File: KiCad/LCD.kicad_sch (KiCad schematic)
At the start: 4 parts

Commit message: Pulling
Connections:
- net SDA is gone; now on net SCL: R2.2, U3.46 (SDA)
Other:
- moved on the sheet: R3

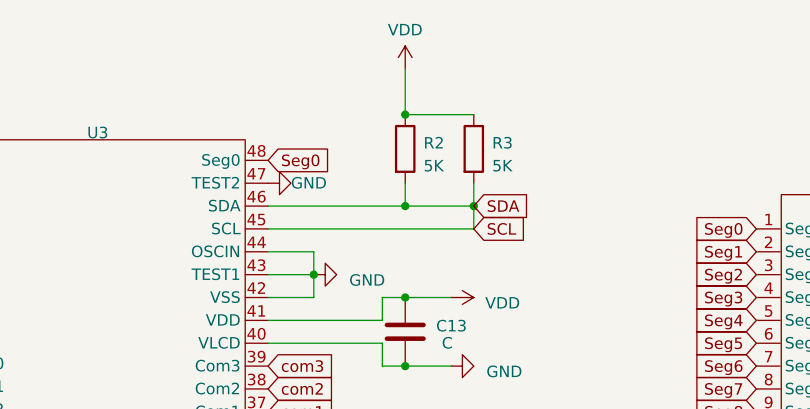
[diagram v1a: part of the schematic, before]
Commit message: Lcd files started.
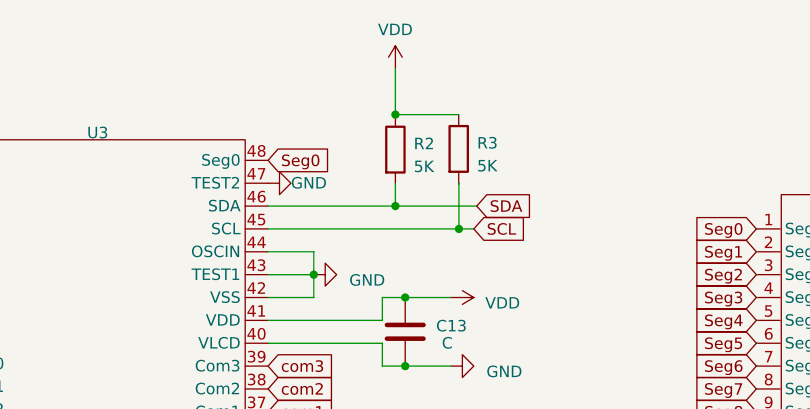
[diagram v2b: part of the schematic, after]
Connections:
- net SCL: no longer R2.2, U3.46 (SDA)
- new net SDA: R2.2, U3.46 (SDA)
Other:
- moved on the sheet: R2, R3
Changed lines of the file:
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@@
     (rev "1.0")
   )
+  (junction (at 125.349 71.12) (diameter 0) (color 0 0 0 0)
+  )
   (junction (at 119.38 78.74) (diameter 0) (color 0 0 0 0)
   )
-  (junction (at 119.38 58.42) (diameter 0) (color 0 0 0 0)
+  (junction (at 118.2878 68.58) (diameter 0) (color 0 0 0 0)
   )
   (junction (at 109.22 76.2) (diameter 0) (color 0 0 0 0)
@@
   (junction (at 119.38 86.36) (diameter 0) (color 0 0 0 0)
   )
-  (junction (at 127 68.58) (diameter 0) (color 0 0 0 0)
-  )
-  (junction (at 119.38 68.58) (diameter 0) (color 0 0 0 0)
+  (junction (at 118.2878 58.42) (diameter 0) (color 0 0 0 0)
   )
   (wire (pts (xy 158.3944 76.2) (xy 158.496 76.2))
@@
     (stroke (width 0) (type default))
   )
-  (wire (pts (xy 127 66.04) (xy 127 68.58))
-    (stroke (width 0) (type default))
-  )
-  (wire (pts (xy 127 68.58) (xy 119.38 68.58))
-    (stroke (width 0) (type default))
-  )
   (wire (pts (xy 158.3944 73.66) (xy 158.496 73.66))
     (stroke (width 0) (type default))
@@
     (stroke (width 0) (type default))
   )
-  (wire (pts (xy 104.14 71.12) (xy 127 71.12))
+  (wire (pts (xy 104.14 71.12) (xy 125.349 71.12))
+    (stroke (width 0) (type default))
+  )
+  (wire (pts (xy 118.2878 58.42) (xy 118.2878 58.4962))
     (stroke (width 0) (type default))
   )
@@
     (stroke (width 0) (type default))
   )
+  (wire (pts (xy 118.2878 58.42) (xy 125.3236 58.42))
+    (stroke (width 0) (type default))
+  )
   (wire (pts (xy 158.3944 104.14) (xy 158.496 104.14))
     (stroke (width 0) (type default))
   )
+  (wire (pts (xy 125.349 71.12) (xy 127 71.12))
+    (stroke (width 0) (type default))
+  )
   (wire (pts (xy 158.3944 86.36) (xy 158.496 86.36))
     (stroke (width 0) (type default))
@@
     (stroke (width 0) (type default))
   )
+  (wire (pts (xy 125.3236 66.0908) (xy 125.3236 66.04))
+    (stroke (width 0) (type default))
+  )
+  (wire (pts (xy 118.2878 53.3146) (xy 118.2878 58.42))
+    (stroke (width 0) (type default))
+  )
   (wire (pts (xy 158.3944 81.28) (xy 158.496 81.28))
     (stroke (width 0) (type default))
   )
+  (wire (pts (xy 125.349 66.0908) (xy 125.3236 66.0908))
+    (stroke (width 0) (type default))
+  )
   (wire (pts (xy 116.84 86.36) (xy 119.38 86.36))
     (stroke (width 0) (type default))
   )
-  (wire (pts (xy 119.38 66.04) (xy 119.38 68.58))
+  (wire (pts (xy 118.2878 66.1162) (xy 118.2878 68.58))
     (stroke (width 0) (type default))
   )
@@
     (stroke (width 0) (type default))
   )
-  (wire (pts (xy 119.38 53.34) (xy 119.38 58.42))
-    (stroke (width 0) (type default))
-  )
-  (wire (pts (xy 119.38 58.42) (xy 127 58.42))
+  (wire (pts (xy 125.349 66.0908) (xy 125.349 71.12))
     (stroke (width 0) (type default))
   )
@@
     (stroke (width 0) (type default))
   )
-  (wire (pts (xy 119.38 68.58) (xy 104.14 68.58))
-    (stroke (width 0) (type default))
-  )
-  (wire (pts (xy 127 68.58) (xy 127 71.12))
+  (wire (pts (xy 118.2878 68.58) (xy 104.14 68.58))
+    (stroke (width 0) (type default))
+  )
+  (wire (pts (xy 118.2878 68.58) (xy 127.3302 68.58))
     (stroke (width 0) (type default))
   )
@@
     )
   )
-  (global_label "SDA" (shape input) (at 127 68.58 0) (fields_autoplaced)
+  (global_label "SDA" (shape input) (at 127.3302 68.58 0) (fields_autoplaced)
     (effects (font (size 1.27 1.27)) (justify left))
     (property "Intersheetrefs" "${INTERSHEET_REFS}" (at 133.4739 68.58 0)
@@
     )
   )
-  (symbol (lib_id "Device:R") (at 119.38 62.23 0) (unit 1)
+  (symbol (lib_id "Device:R") (at 118.2878 62.3062 0) (unit 1)
     (in_bom yes) (on_board yes) (dnp no) (fields_autoplaced)
-    (property "Reference" "R2" (at 121.412 61.595 0)
+    (property "Reference" "R2" (at 120.3198 61.6712 0)
       (effects (font (size 1.27 1.27)) (justify left))
     )
-    (property "Value" "5K" (at 121.412 64.135 0)
+    (property "Value" "5K" (at 120.3198 64.2112 0)
       (effects (font (size 1.27 1.27)) (justify left))
     )
-    (property "Footprint" "" (at 117.602 62.23 90)
-      (effects (font (size 1.27 1.27)) hide)
-    )
-    (property "Datasheet" "~" (at 119.38 62.23 0)
+    (property "Footprint" "" (at 116.5098 62.3062 90)
+      (effects (font (size 1.27 1.27)) hide)
+    )
+    (property "Datasheet" "~" (at 118.2878 62.3062 0)
       (effects (font (size 1.27 1.27)) hide)
     )
@@
     )
   )
-  (symbol (lib_id "Device:R") (at 127 62.23 0) (unit 1)
+  (symbol (lib_id "Device:R") (at 125.3236 62.23 0) (unit 1)
     (in_bom yes) (on_board yes) (dnp no) (fields_autoplaced)
-    (property "Reference" "R3" (at 129.032 61.595 0)
+    (property "Reference" "R3" (at 127.3556 61.595 0)
       (effects (font (size 1.27 1.27)) (justify left))
     )
-    (property "Value" "5K" (at 129.032 64.135 0)
+    (property "Value" "5K" (at 127.3556 64.135 0)
       (effects (font (size 1.27 1.27)) (justify left))
     )
-    (property "Footprint" "" (at 125.222 62.23 90)
-      (effects (font (size 1.27 1.27)) hide)
-    )
-    (property "Datasheet" "~" (at 127 62.23 0)
+    (property "Footprint" "" (at 123.5456 62.23 90)
+      (effects (font (size 1.27 1.27)) hide)
+    )
+    (property "Datasheet" "~" (at 125.3236 62.23 0)
       (effects (font (size 1.27 1.27)) hide)
     )
@@
     )
   )
-  (symbol (lib_id "power:VDD") (at 119.38 53.34 0) (unit 1)
+  (symbol (lib_id "power:VDD") (at 118.2878 53.3146 0) (unit 1)
     (in_bom yes) (on_board yes) (dnp no) (fields_autoplaced)
-    (property "Reference" "#PWR011" (at 119.38 57.15 0)
-      (effects (font (size 1.27 1.27)) hide)
-    )
-    (property "Value" "VDD" (at 119.38 49.022 0)
+    (property "Reference" "#PWR011" (at 118.2878 57.1246 0)
+      (effects (font (size 1.27 1.27)) hide)
+    )
+    (property "Value" "VDD" (at 118.2878 48.9966 0)
       (effects (font (size 1.27 1.27)))
     )
-    (property "Footprint" "" (at 119.38 53.34 0)
-      (effects (font (size 1.27 1.27)) hide)
-    )
-    (property "Datasheet" "" (at 119.38 53.34 0)
-      (effects (font (size 1.27 1.27)) hide)
-    )
+    (property "Footprint" "" (at 118.2878 53.3146 0)
+      (effects (font (size 1.27 1.27)) hide)
+    )
+    (property "Datasheet" "" (at 118.2878 53.3146 0)
+      (effects (font (size 1.27 1.27)) hide)
+    )

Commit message: Ki cad schematic update.
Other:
- moved on the sheet: R2
